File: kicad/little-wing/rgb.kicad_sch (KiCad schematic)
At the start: 7 parts, among them J3 rgb, Q1 AO3401A, Q2 2N7002

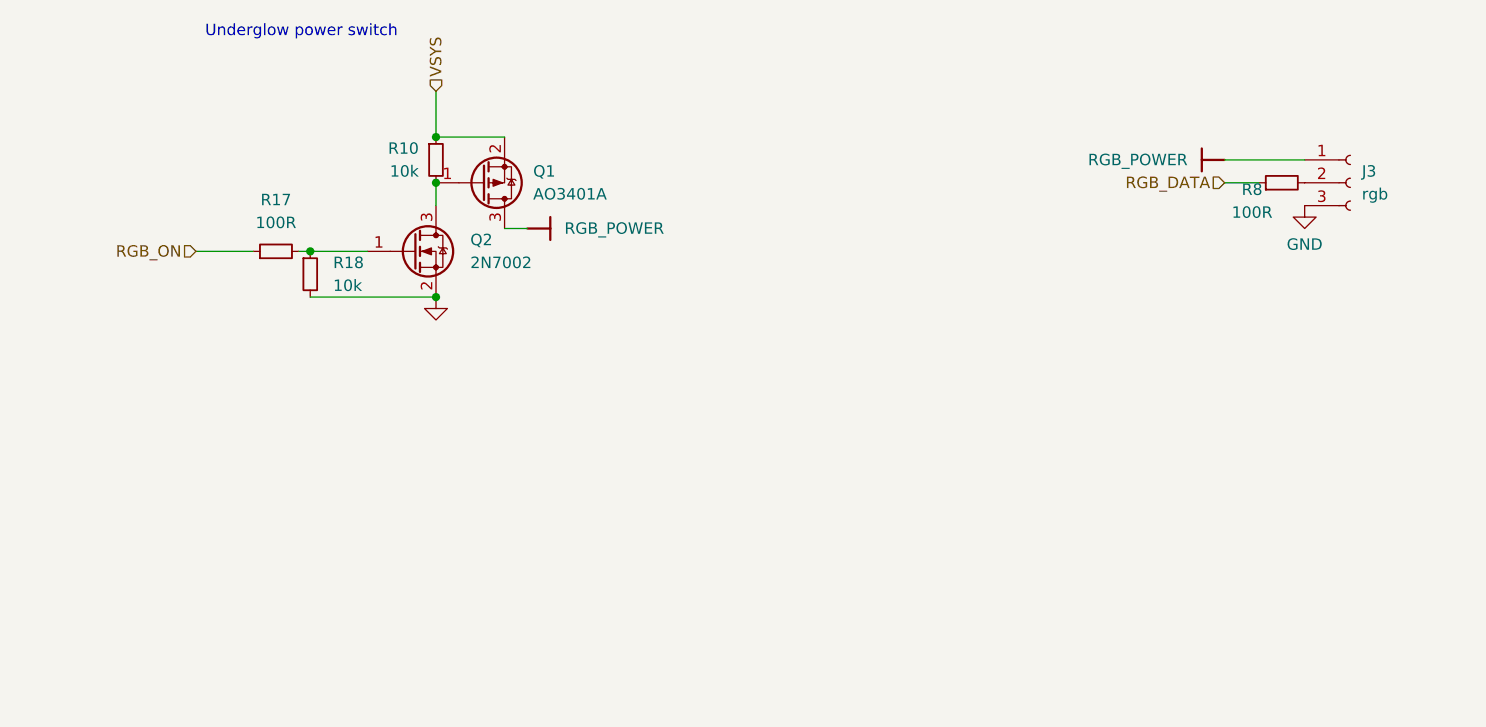
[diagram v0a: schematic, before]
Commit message: Reworking the RGB power section
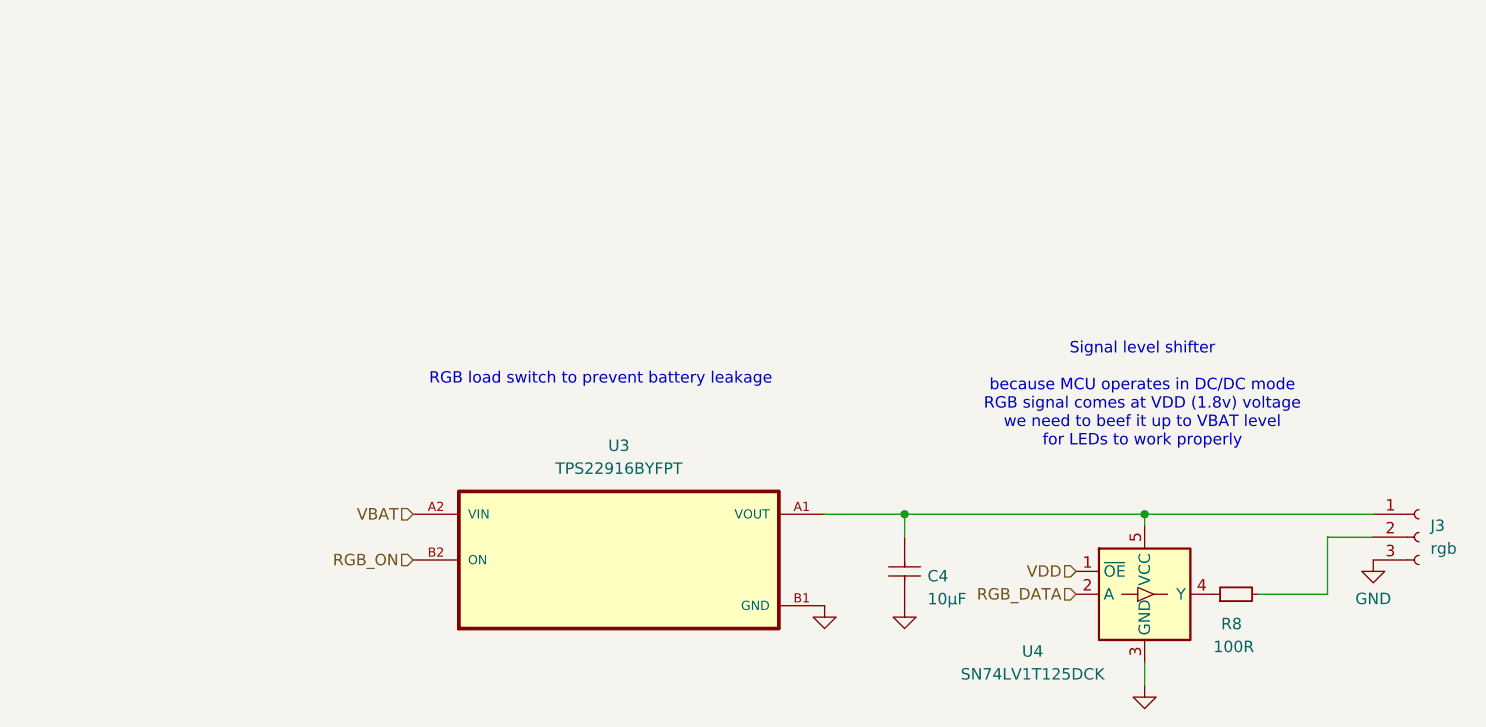
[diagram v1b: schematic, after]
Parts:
- removed Q1: AO3401A, Package_TO_SOT_SMD:SOT-323_SC-70, symbol Transistor_FET:AO3401A
- removed Q2: 2N7002, Package_TO_SOT_SMD:SOT-523, symbol Transistor_FET:2N7002
- removed R10, R18: 10k, Resistor_SMD:R_0201_0603Metric, symbol Device:R_Small
- removed R17: 100R, Resistor_SMD:R_0201_0603Metric, symbol Device:R_Small
- added C4: 10µF, Passive:CAPC1608X06L, symbol Nordic Passive DB:root_1_CAP_Nordic Passive DB.DbLib
- added U3: TPS22916BYFPT, TPS22916 load switch:BGA4C40P2X2_77X77X50, symbol TPS22916 load switch:TPS22916BYFPT
- added U4: SN74LV1T125DCK, Package_TO_SOT_SMD:SOT-353_SC-70-5, symbol Logic_LevelTranslator:SN74LV1T125DCK
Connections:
- net GND: now also C4.1, U3.B1 (GND), U4.3 (GND)
- net RGB_DATA: now also U4.2 (A); no longer R8.1
- net RGB_ON: now also U3.B2 (ON)
- net RGB_POWER: no longer names the net of J3.1 (Pin_1)
- net RGB_POWER: now also C4.2, U3.A1 (VOUT), U4.5 (VCC)
- new net: R8.1, U4.4 (Y)
- new net VBAT: U3.A2 (VIN)
- new net VDD: U4.1 (~{OE})
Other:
- note added: "RGB load switch to prevent battery leakage"
- note added: "Signal level shifter because MCU operates in DC/DC mode RGB signal comes at VDD (1.8v) voltage we need to beef it up to VBAT level for LEDs to work properly"
- note removed: "Underglow power switch"
- moved on the sheet: J3, R8

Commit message: Moving the RGB feed capacitor
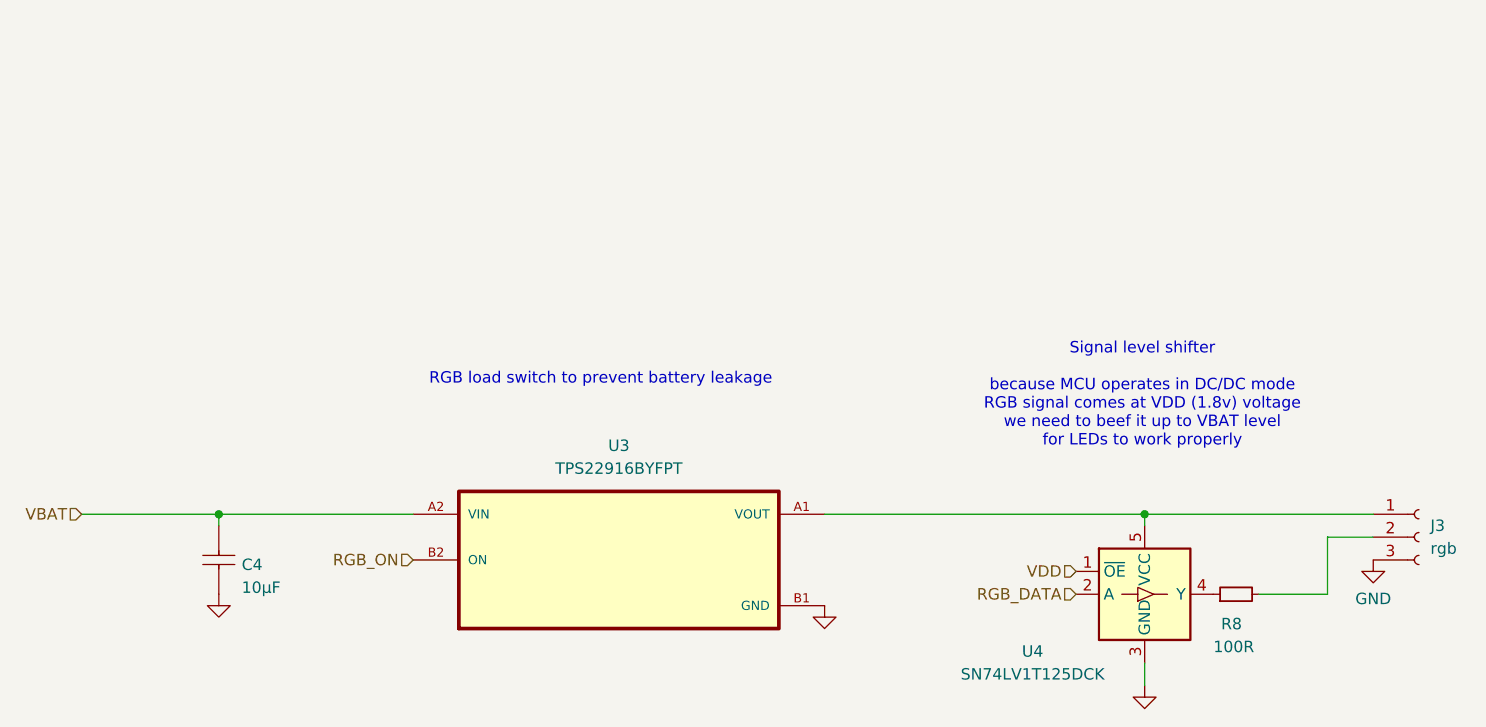
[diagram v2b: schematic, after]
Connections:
- net VBAT: now also C4.2
- net at J3.1 (Pin_1), U3.A1 (VOUT), U4.5 (VCC): no longer C4.2
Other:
- moved on the sheet: C4
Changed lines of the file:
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@@
-	)
-	(junction
-		(at 142.24 97.79)
-		(diameter 0)
-		(color 0 0 0 0)
 	)
 	(junction
@@
 		(color 0 0 0 0)
 	)
+	(junction
+		(at 66.04 97.79)
+		(diameter 0)
+		(color 0 0 0 0)
+	)
 	(wire
 		(pts
-			(xy 142.24 97.79) (xy 142.24 100.33)
+			(xy 66.04 97.79) (xy 87.63 97.79)
 		)
 		(stroke
@@
 	(wire
 		(pts
-			(xy 168.91 97.79) (xy 168.91 99.06)
+			(xy 66.04 97.79) (xy 66.04 99.06)
 		)
 		(stroke
@@
 	(wire
 		(pts
-			(xy 168.91 97.79) (xy 194.31 97.79)
+			(xy 168.91 97.79) (xy 168.91 99.06)
 		)
 		(stroke
@@
 	(wire
 		(pts
-			(xy 133.35 97.79) (xy 142.24 97.79)
+			(xy 168.91 97.79) (xy 194.31 97.79)
 		)
 		(stroke
@@
 	(wire
 		(pts
-			(xy 189.23 100.33) (xy 194.31 100.33)
+			(xy 133.35 97.79) (xy 168.91 97.79)
 		)
 		(stroke
@@
 	(wire
 		(pts
-			(xy 142.24 97.79) (xy 168.91 97.79)
+			(xy 189.23 100.33) (xy 194.31 100.33)
+		)
+		(stroke
+			(width 0)
+			(type default)
+		)
+	)
+	(wire
+		(pts
+			(xy 50.8 97.79) (xy 66.04 97.79)
 		)
 		(stroke
@@
 	(hierarchical_label "VBAT"
 		(shape input)
-		(at 87.63 97.79 180)
+		(at 50.8 97.79 180)
 		(effects
 			(font
@@
 	(symbol
 		(lib_id "power:GND")
-		(at 142.24 107.95 0)
+		(at 66.04 106.68 0)
 		(unit 1)
 		(exclude_from_sim no)
@@
 		(fields_autoplaced yes)
 		(property "Reference" "#PWR0151"
-			(at 142.24 114.3 0)
+			(at 66.04 113.03 0)
 			(effects
 				(font
@@
 		)
 		(property "Value" "GND"
-			(at 144.78 109.0294 0)
+			(at 68.58 107.7594 0)
 			(effects
 				(font
@@
 		)
 		(property "Footprint" ""
-			(at 142.24 107.95 0)
+			(at 66.04 106.68 0)
 			(effects
 				(font
@@
 		)
 		(property "Datasheet" ""
-			(at 142.24 107.95 0)
+			(at 66.04 106.68 0)
 			(effects
 				(font
@@
 		)
 		(property "Description" ""
-			(at 142.24 107.95 0)
+			(at 66.04 106.68 0)
 			(effects
 				(font
@@
 		(lib_name "root_1_CAP_Nordic Passive DB.DbLib_1")
 		(lib_id "Nordic Passive DB:root_1_CAP_Nordic Passive DB.DbLib")
-		(at 142.24 107.95 0)
+		(at 66.04 106.68 0)
 		(unit 1)
 		(exclude_from_sim no)
@@
 		(dnp no)
 		(property "Reference" "C4"
-			(at 144.78 105.41 0)
+			(at 68.58 104.14 0)
 			(effects
 				(font
@@
 		)
 		(property "Value" "10µF"
-			(at 144.78 107.95 0)
+			(at 68.58 106.68 0)
 			(effects
 				(font
@@
 		)
 		(property "Footprint" "Passive:CAPC1608X06L"
-			(at 142.24 107.95 0)
+			(at 66.04 106.68 0)
 			(effects
 				(font
@@
 		)
 		(property "Datasheet" ""
-			(at 142.24 107.95 0)
+			(at 66.04 106.68 0)
 			(effects
 				(font
@@
 		)
 		(property "Description" "Capacitor, X7R, ±10%"
-			(at 142.24 107.95 0)
+			(at 66.04 106.68 0)
 			(effects
 				(font
@@
 		)
 		(property "PART NUMBER" "C0603-1µ0"
-			(at 140.97 104.14 0)
+			(at 64.77 102.87 0)
 			(effects
 				(font
@@
 		)
 		(property "LATESTREVISIONDATE" "2013-06-05"
-			(at 140.97 104.14 0)
+			(at 64.77 102.87 0)
 			(effects
 				(font
@@
 		)
 		(property "PIN COUNT" "2"
-			(at 140.97 104.14 0)
+			(at 64.77 102.87 0)
 			(effects
 				(font
@@
 		)
 		(property "PUBLISHER" "Nordic Semiconductor"
-			(at 140.97 104.14 0)
+			(at 64.77 102.87 0)
 			(effects
 				(font
@@
 		)
 		(property "PUBLISHED" "2009-05-08"
-			(at 140.97 104.14 0)
+			(at 64.77 102.87 0)
 			(effects
 				(font
@@
 		)
 		(property "ALTIUM_VALUE" "1.0µF"
-			(at 140.97 104.14 0)
+			(at 64.77 102.87 0)
 			(effects
 				(font
@@
 		)
 		(property "FOOTPRINT DOC" "0603"
-			(at 144.78 110.49 0)
+			(at 68.58 109.22 0)
 			(effects
 				(font
@@
 		)
 		(property "ASSEMBLY" ""
-			(at 140.208 99.822 0)
+			(at 64.008 98.552 0)
 			(effects
 				(font
@@
 		)
 		(property "MANUFACTURER" "*"
-			(at 140.97 101.6 0)
+			(at 64.77 100.33 0)
 			(effects
 				(font
@@
 		)
 		(property "MANUFACTURER PART NUMBER" "*"
-			(at 140.97 101.6 0)
-			(effects
-				(font
+			(at 64.77 100.33 0)
+			(effects
+				(font

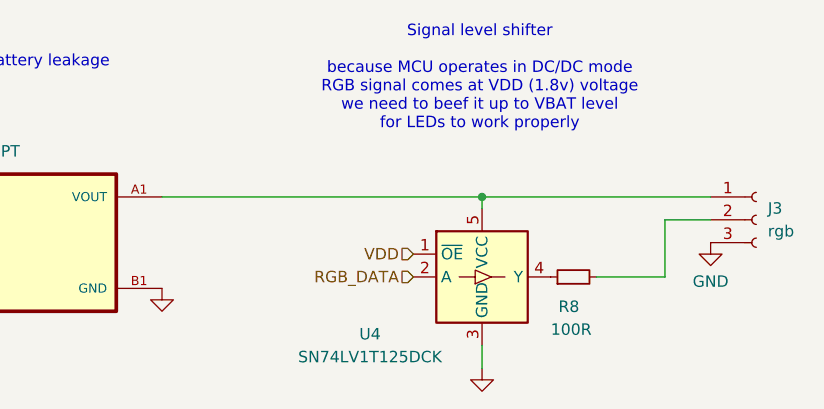
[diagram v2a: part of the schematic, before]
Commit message: Removing the RGB level shifter
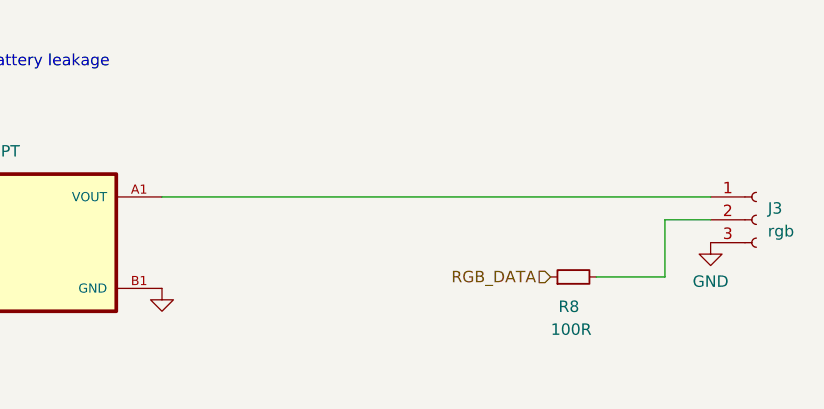
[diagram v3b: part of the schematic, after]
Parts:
- removed U4: SN74LV1T125DCK, Package_TO_SOT_SMD:SOT-353_SC-70-5, symbol Logic_LevelTranslator:SN74LV1T125DCK
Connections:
- net RGB_DATA: now also R8.1
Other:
- note removed: "Signal level shifter because MCU operates in DC/DC mode RGB signal comes at VDD (1.8v) voltage we need to beef it up to VBAT level for LEDs to work properly"
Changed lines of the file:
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@@
 		)
-	)
-	(text "Signal level shifter\n\nbecause MCU operates in DC/DC mode\nRGB signal comes at VDD (1.8v) voltage\nwe need to beef it up to VBAT level\nfor LEDs to work properly"
-		(exclude_from_sim no)
-		(at 168.656 84.582 0)
-		(effects
-			(font
-				(size 1.27 1.27)
-			)
-		)
-	)
-	(junction
-		(at 168.91 97.79)
-		(diameter 0)
-		(color 0 0 0 0)
 	)
 	(junction
@@
 	(wire
 		(pts
-			(xy 168.91 97.79) (xy 168.91 99.06)
-		)
-		(stroke
-			(width 0)
-			(type default)
-		)
-	)
-	(wire
-		(pts
-			(xy 168.91 97.79) (xy 194.31 97.79)
-		)
-		(stroke
-			(width 0)
-			(type default)
-		)
-	)
-	(wire
-		(pts
-			(xy 133.35 97.79) (xy 168.91 97.79)
+			(xy 133.35 97.79) (xy 194.31 97.79)
 		)
 		(stroke
@@
 	(wire
 		(pts
-			(xy 168.91 114.3) (xy 168.91 116.84)
-		)
-		(stroke
-			(width 0)
-			(type default)
-		)
-	)
-	(wire
-		(pts
 			(xy 181.61 106.68) (xy 189.23 106.68)
 		)
@@
 			(width 0)
 			(type default)
-		)
-	)
-	(hierarchical_label "VDD"
-		(shape input)
-		(at 161.29 104.14 180)
-		(effects
-			(font
-				(size 1.27 1.27)
-			)
-			(justify right)
 		)
 	)
@@
 	(hierarchical_label "RGB_DATA"
 		(shape input)
-		(at 161.29 106.68 180)
+		(at 176.53 106.68 180)
 		(effects
 			(font
@@
 	)
 	(symbol
-		(lib_id "Logic_LevelTranslator:SN74LV1T125DCK")
-		(at 168.91 106.68 0)
-		(unit 1)
-		(exclude_from_sim no)
-		(in_bom yes)
-		(on_board yes)
-		(dnp no)
-		(property "Reference" "U4"
-			(at 156.464 113.03 0)
-			(effects
-				(font
-					(size 1.27 1.27)
-				)
-			)
-		)
-		(property "Value" "SN74LV1T125DCK"
-			(at 156.464 115.57 0)
-			(effects
-				(font
-					(size 1.27 1.27)
-				)
-			)
-		)
-		(property "Footprint" "Package_TO_SOT_SMD:SOT-353_SC-70-5"
-			(at 168.91 130.81 0)
-			(effects
-				(font
-					(size 1.27 1.27)
-				)
-				(hide yes)
-			)
-		)
-		(property "Datasheet" "https://www.ti.com/lit/ds/symlink/sn74lv1t125.pdf"
-			(at 168.91 128.27 0)
-			(effects
-				(font
-					(size 1.27 1.27)
-				)
-				(hide yes)
-			)
-		)
-		(property "Description" "Single Power Supply, Single Buffer Gate with 3-State Output, CMOS Logic Level Shifter Level Shifter, SC70-5"
-			(at 168.91 106.68 0)
-			(effects
-				(font
-					(size 1.27 1.27)
-				)
-				(hide yes)
-			)
-		)
-		(pin "2"
-		)
-		(pin "4"
-		)
-		(pin "1"
-		)
-		(pin "5"
-		)
-		(pin "3"
-		)
-		(instances
-			(project ""
-				(path "/3a835e6f-a660-4b38-a102-87841cdd95ed/95df33f4-bbca-475a-b4f9-9e753f1a5f8c"
-					(reference "U4")
-					(unit 1)
-				)
-			)
-		)
-	)
-	(symbol
 		(lib_id "power:GND")
 		(at 66.04 106.68 0)
@@
 					(unit 1)
 				)
-			)
-		)
-	)
-	(symbol
-		(lib_id "power:GND")
-		(at 168.91 116.84 0)
-		(unit 1)
-		(exclude_from_sim no)
-		(in_bom yes)
-		(on_board yes)
-		(dnp no)
-		(fields_autoplaced yes)
-		(property "Reference" "#PWR0152"
-			(at 168.91 123.19 0)
-			(effects
-				(font
-					(size 1.27 1.27)
-				)
-				(hide yes)
-			)
-		)
-		(property "Value" "GND"
-			(at 171.45 117.9194 0)
-			(effects
-				(font
-					(size 1.27 1.27)
-				)
-				(justify left)
-				(hide yes)
-			)
-		)
-		(property "Footprint" ""
-			(at 168.91 116.84 0)
-			(effects
-				(font
-					(size 1.27 1.27)
-				)
-				(hide yes)
-			)
-		)
-		(property "Datasheet" ""
-			(at 168.91 116.84 0)
-			(effects
-				(font
-					(size 1.27 1.27)
-				)
-				(hide yes)
-			)
-		)
-		(property "Description" ""
-			(at 168.91 116.84 0)
-			(effects
-				(font
-					(size 1.27 1.27)
-				)
-				(hide yes)
-			)
-		)
-		(pin "1"
-		)
-		(instances
-			(project "little-wing"
-				(path "/3a835e6f-a660-4b38-a102-87841cdd95ed/95df33f4-bbca-475a-b4f9-9e753f1a5f8c"
-					(reference "#PWR0152")
-					(unit 1)
-				)
